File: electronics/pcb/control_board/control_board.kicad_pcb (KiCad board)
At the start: 2 copper layers, 100 x 100 mm, 31 parts, among them J1 Motor M1X, J10 Test (Analog Discovery), J2 Motor M1Y, J3 Motor M2X, J4 Motor M2Y, J5 12V IN, J6 12V IN 5.5x2.1, J7 Laser, J8 PD reference, J9 PD output, U1 TMC2209 M1X (addr 0), U2 TMC2209 M1Y (addr 1), U3 TMC2209 M2X (addr 2), U4 TMC2209 M2Y (addr 3)

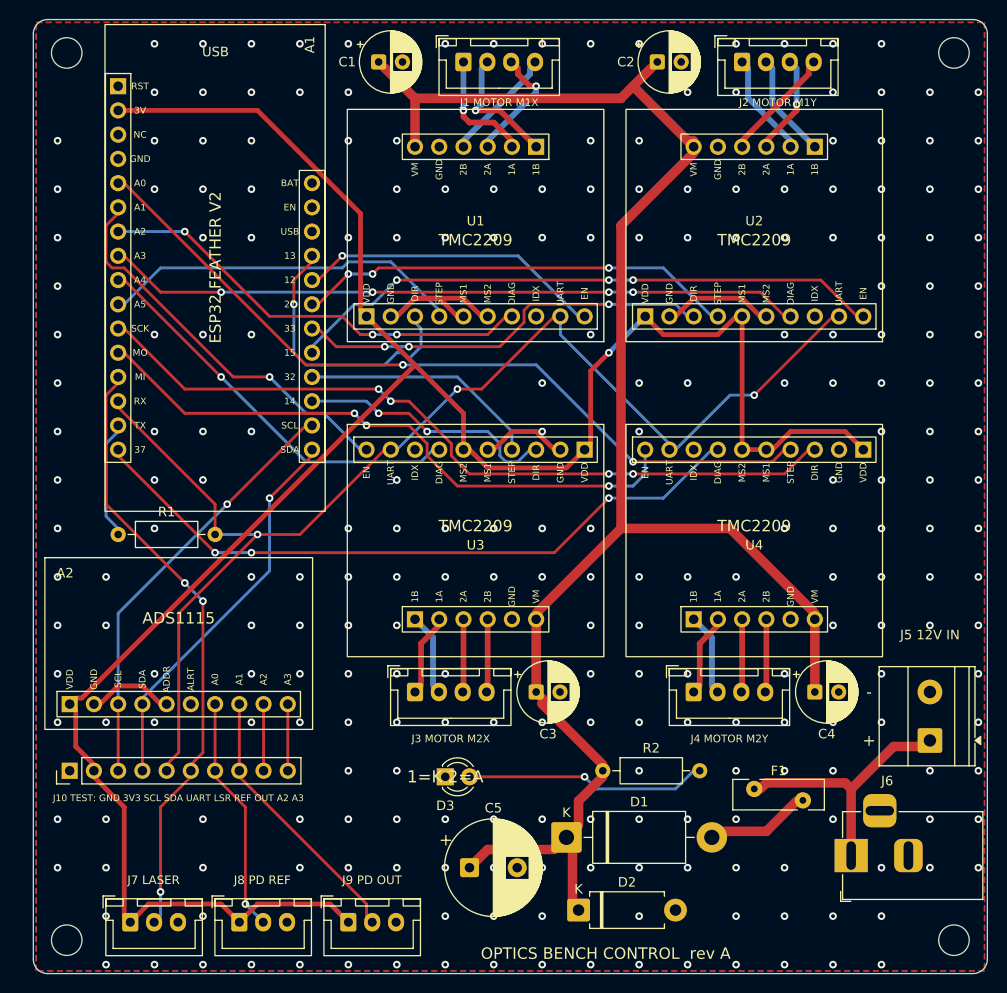
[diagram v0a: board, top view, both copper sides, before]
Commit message: Keep the TMC2209 screw terminals on the control board
The breakouts now plug in by their 10-pin logic header only and keep their
screw terminals. The top pair sits with its terminals on the top edge and
the bottom pair on the bottom edge, so the motor and VM wires come in from
outside the board. Two M2 standoff holes sit under each breakout's
terminal-end mounting holes.

The JST-XH motor plugs are gone. A 2-pin VM plug (J1-J4) and a 100 uF
capacitor next to each driver feed the breakout's VM terminals over a
short lead. The power input, test header and VM plugs moved into the
middle of the board, which is still 100 x 100 mm.

A thin ground tree under the pours keeps every pour piece connected.
The socket footprints now carry the female header 3D models, so the
render shows them. ERC and DRC with schematic parity report no errors.
The wiring docs, system diagram and BOM are updated to match.
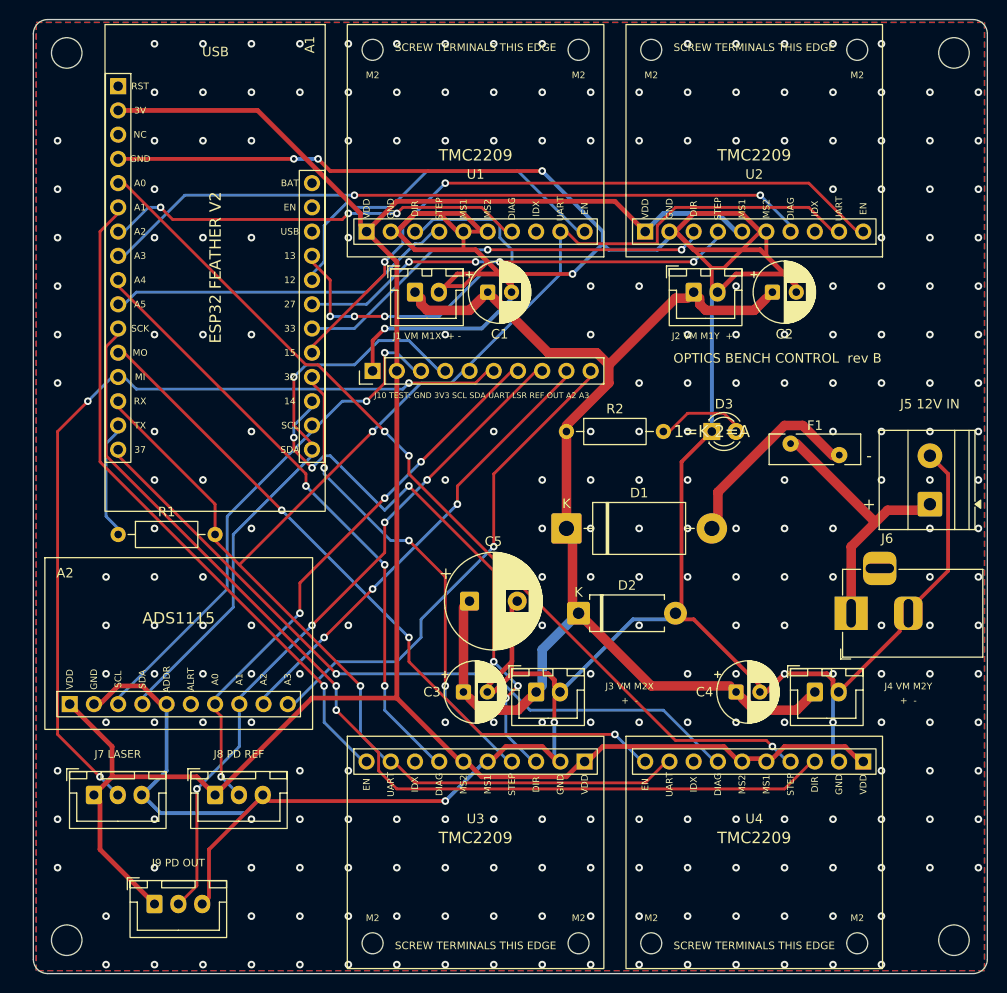
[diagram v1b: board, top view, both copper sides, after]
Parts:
- J1: value Motor M1X -> VM M1X; footprint Connector_JST:JST_XH_B4B-XH-A_1x04_P2.50mm_Vertical -> Connector_JST:JST_XH_B2B-XH-A_1x02_P2.50mm_Vertical
- J2: value Motor M1Y -> VM M1Y; footprint Connector_JST:JST_XH_B4B-XH-A_1x04_P2.50mm_Vertical -> Connector_JST:JST_XH_B2B-XH-A_1x02_P2.50mm_Vertical
- J3: value Motor M2X -> VM M2X; footprint Connector_JST:JST_XH_B4B-XH-A_1x04_P2.50mm_Vertical -> Connector_JST:JST_XH_B2B-XH-A_1x02_P2.50mm_Vertical
- J4: value Motor M2Y -> VM M2Y; footprint Connector_JST:JST_XH_B4B-XH-A_1x04_P2.50mm_Vertical -> Connector_JST:JST_XH_B2B-XH-A_1x02_P2.50mm_Vertical
- moved J10 52.6 mm to (35.6, 36.8)
- moved D3 45.7 mm to (71.1, 43.2)
- moved F1 36.4 mm to (79.4, 44.5)
- moved R2 35.8 mm to (55.9, 43.2)
- moved U3 32.7 mm to (57.8, 77.8)
- moved U4 32.7 mm to (87.0, 77.8)
- moved D1 32.4 mm to (55.9, 53.3)
- moved D2 31.1 mm to (57.1, 62.2)
- moved C5 27.9 mm to (45.7, 61.0)
- moved C2 27.0 mm to (77.5, 28.6)
- moved C1 26.7 mm to (47.6, 28.6)
- moved J6 25.4 mm to (85.7, 62.2)
- moved J5 24.8 mm to (94.0, 50.8)
- moved J1 24.7 mm to (40.0, 28.6)
- moved J2 24.7 mm to (69.2, 28.6)
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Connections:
- J1 pad 1: /M1X_1A -> +12V
- J1 pad 2: /M1X_1B -> GND
- J2 pad 1: /M1Y_1A -> +12V
- J2 pad 2: /M1Y_1B -> GND
- J3 pad 1: /M2X_1A -> +12V
- J3 pad 2: /M2X_1B -> GND
- J4 pad 1: /M2Y_1A -> +12V
- J4 pad 2: /M2Y_1B -> GND
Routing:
- net GND: track 44.7 -> 443.7 mm, vias 255 -> 260
- net +12V: track 165.8 -> 115.8 mm
- net /AIN3: track 5.72 -> 50.9 mm, vias 0 -> 1
- net /PD_OUT: track 25.8 -> 69.2 mm, vias 0 -> 4
- net /AIN2: track 5.72 -> 46.8 mm, vias 0 -> 3
- net /PD_REF: track 22.2 -> 56.2 mm, vias 1 -> 4
- net /M2X_DIR: track 26.1 -> 56.9 mm, vias 2 -> 6
- net /TMC_UART: track 127.8 -> 158.1 mm, vias 3 -> 2
- net /M2X_EN: track 40.4 -> 69.2 mm
- net /LASER_TTL: track 61.2 -> 87.3 mm
- net /M2Y_DIR: track 79.9 -> 105.0 mm, vias 4 -> 2
- net /M2X_STEP: track 24.0 -> 48.9 mm, vias 0 -> 3
- net /M2X_DIAG: track 40.8 -> 63.2 mm, vias 1 -> 3
- net /I2C_SDA: track 38.5 -> 58.7 mm
- net /LED_12V: track 24.2 -> 8.30 mm, vias 1 -> 0
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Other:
- board text added: "+ -"
- board text added: "J1 VM M1X + -"
- board text added: "J2 VM M1Y + -"
- board text added: "J3 VM M2X"
- board text added: "J4 VM M2Y"
- board text added: "OPTICS BENCH CONTROL rev B"
- board text removed: "J1 MOTOR M1X"
- board text removed: "J2 MOTOR M1Y"
- board text removed: "J3 MOTOR M2X"
- board text removed: "J4 MOTOR M2Y"
- board text removed: "OPTICS BENCH CONTROL rev A"
